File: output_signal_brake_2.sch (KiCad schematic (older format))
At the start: 37 parts

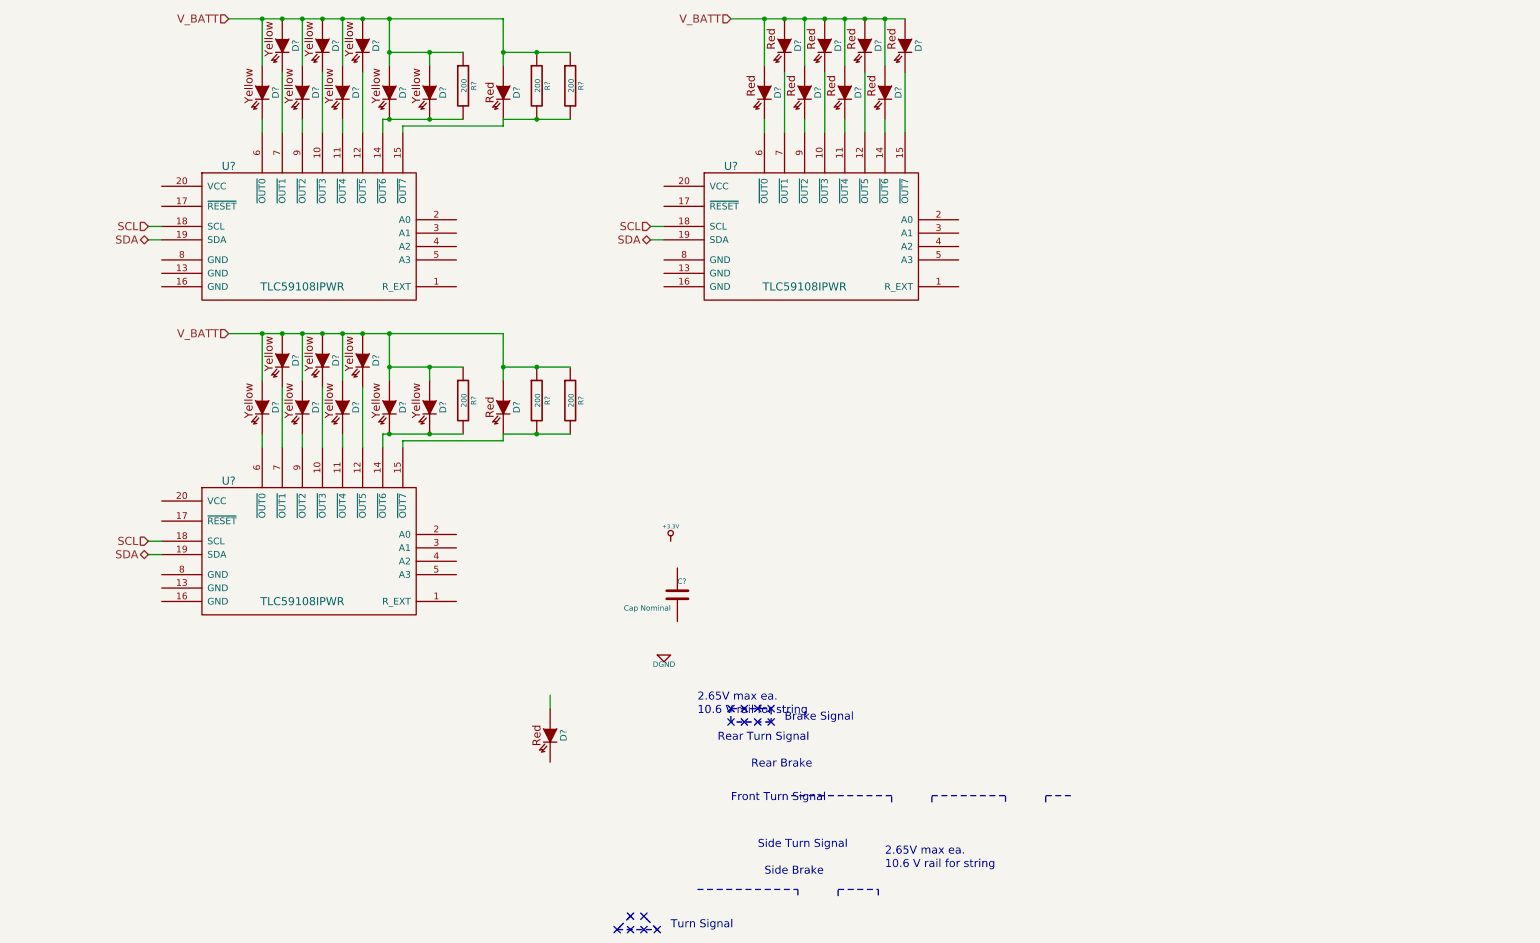
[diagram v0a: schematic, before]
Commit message: finished batt-current LED driver array over I2C
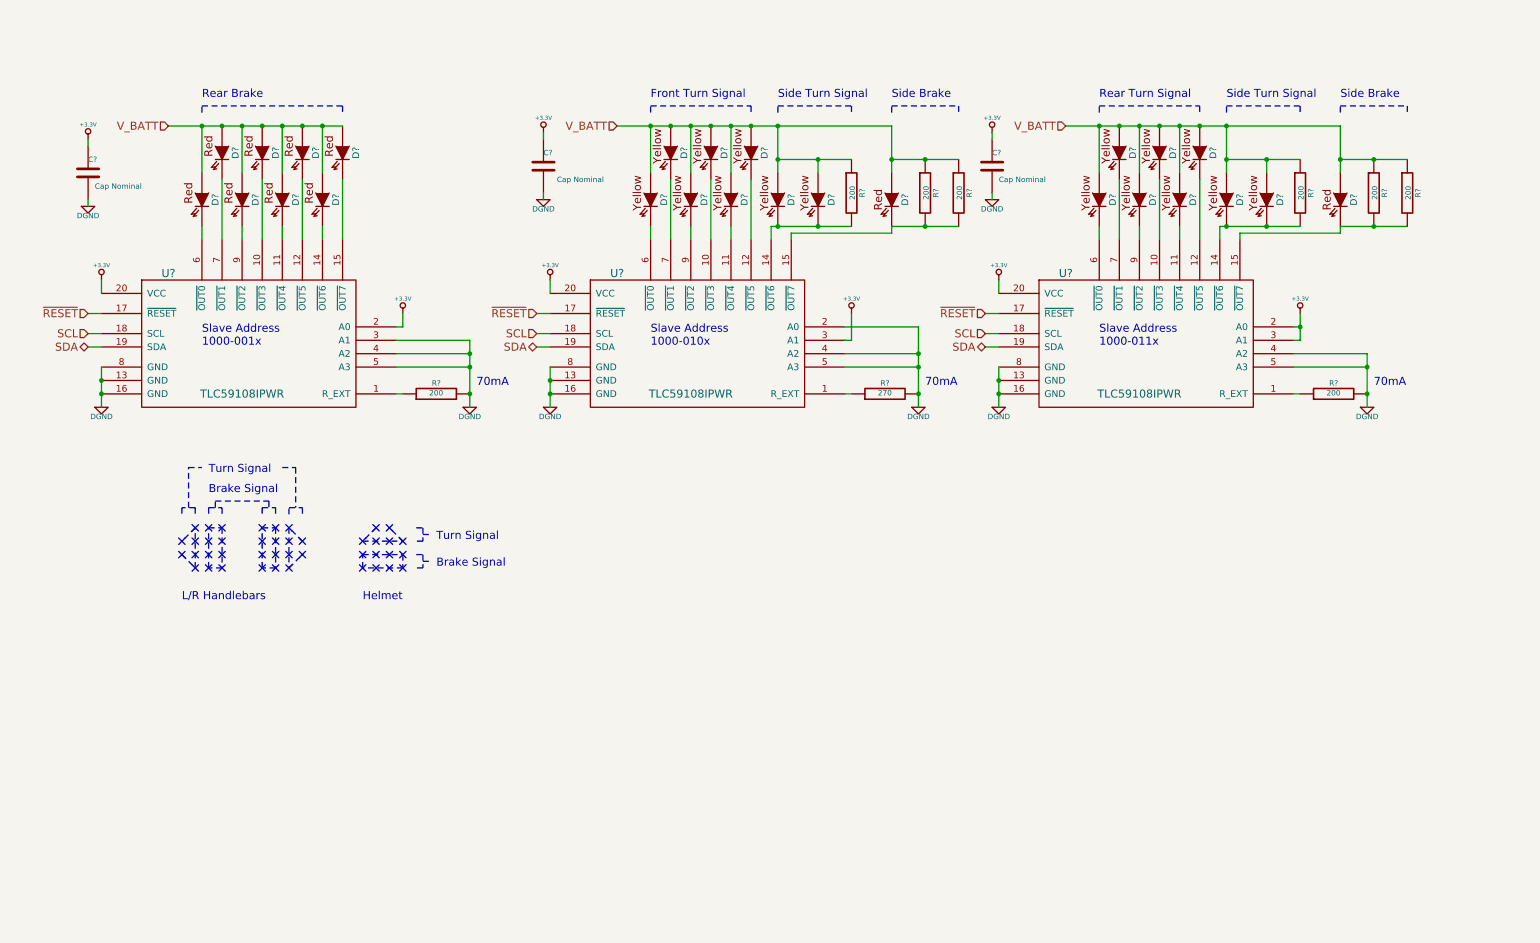
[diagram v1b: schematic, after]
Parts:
- removed D?: LR-A67F, ~, symbol LR-A67F
- added C? (x2): Cap Nominal, ~, symbol C
- added R?: 270, ~, symbol R
- added R? (x2): 200, ~, symbol R
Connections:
- net +3.3V: now also C?.1, U?.2 (A0), U?.2 (A0), U?.20 (VCC), U?.20 (VCC), U?.20 (VCC), U?.3 (A1), U?.3 (A1), C?.1, C?.1
- net DGND: now also C?.2, U?.13 (GND), U?.13 (GND), U?.13 (GND), U?.16 (GND), U?.16 (GND), U?.16 (GND), U?.2 (A0), U?.3 (A1), U?.4 (A2), U?.4 (A2), U?.4 (A2), U?.5 (A3), U?.5 (A3), U?.5 (A3), U?.8 (GND), U?.8 (GND), U?.8 (GND), C?.2, C?.2, R?.2, R?.2, R?.2
- net at U?.1 (R_EXT): now also R?.1 (x3)
- net ~RESET: now reaches U?.17 (~RESET)
- net ~RESET: now also U?.17 (~RESET), U?.17 (~RESET)
- no-connect marks 14 -> 42
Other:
- note added: "70mA"
- note added: "Helmet"
- note added: "L/R Handlebars"
- note added: "Slave Address\n1000-001x"
- note added: "Slave Address\n1000-010x"
- note added: "Slave Address\n1000-011x"
- note removed: "10.6 V rail for string"
- note removed: "2.65V max ea."
- moved on the sheet: C?, D?, R?, U?

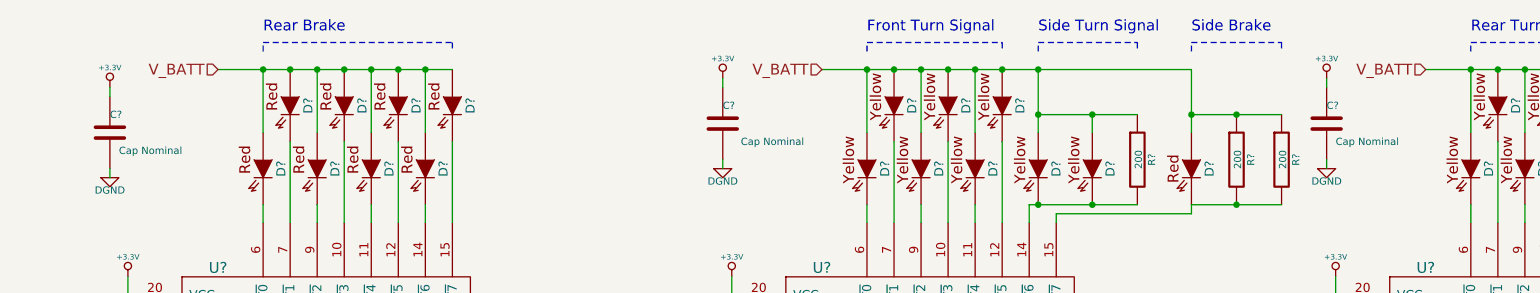
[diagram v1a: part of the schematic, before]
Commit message: added headlight sheet, led, dac
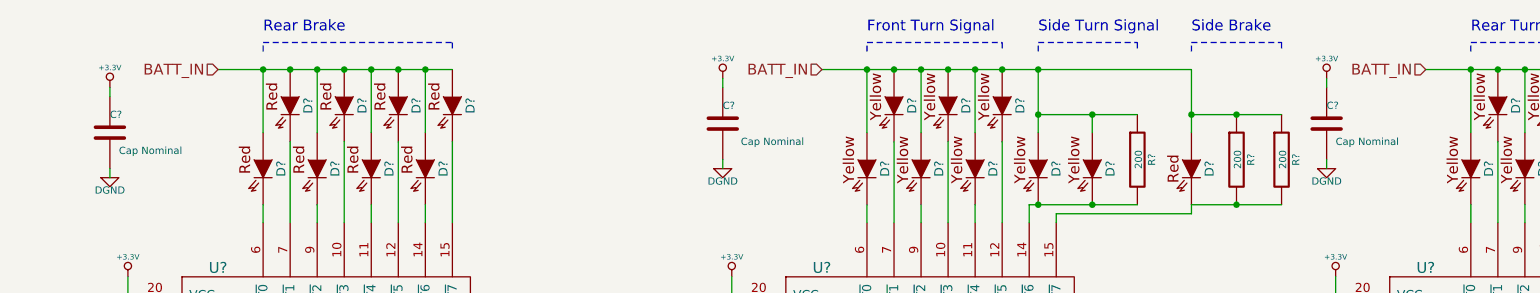
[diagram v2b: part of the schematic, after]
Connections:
- net V_BATT renamed BATT_IN
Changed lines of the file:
@@
 $Descr A4 11693 8268
 encoding utf-8
-Sheet 16 16
+Sheet 16 17
 Title ""
-Date "6 dec 2013"
+Date "7 dec 2013"
 Rev ""
 Comp ""
@@
 $EndComp
 Text HLabel 1500 1400 0    60   Input ~ 0
-V_BATT
+BATT_IN
 $Comp
 L R R?
@@
 	0    1    1    0
 $EndComp
-Text HLabel 8200 1400 0    60   Input ~ 0
-V_BATT
 $Comp
 L R R?
@@
 	0    1    1    0
 $EndComp
-Text HLabel 4850 1400 0    60   Input ~ 0
-V_BATT
 $Comp
 L R R?
@@
 Text Notes 3500 4700 0    60   ~ 0
 Brake Signal
+Text HLabel 4850 1400 0    60   Input ~ 0
+BATT_IN
+Text HLabel 8200 1400 0    60   Input ~ 0
+BATT_IN
 $EndSCHEMATC

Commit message: 2.5V Regulator finished.
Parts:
- added C? (x2): 22uF, ~, symbol CSMALL
- added C? (x2): 10nF, ~, symbol CSMALL
- added L?: 1uH, ~, symbol INDUCTOR
- added R?: 160k, ~, symbol RSMALL
- added R?: 75k, ~, symbol RSMALL
- added R?: 470k, ~, symbol RSMALL
- added U?: TPS62090, ~, symbol TPS62090
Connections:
- net labels added: +2.5V, +BATT, GND
- wire segments 97 -> 139
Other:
- note added: "Battery to 2.5V Buck Power Supply"

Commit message: added thermal pad to 2.5V, added some labels
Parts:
- R? (x2): value 200 -> 270
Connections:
- wire segments 139 -> 138
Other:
- note added: "Don't think we need this output\nor the pull up here. We aren't reading it...?"
- note added: "This needs to be connected."
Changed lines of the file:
@@
 P 10200 3400
 F 0 "R?" V 10280 3400 40  0000 C CNN
-F 1 "200" V 10207 3401 40  0000 C CNN
+F 1 "270" V 10207 3401 40  0000 C CNN
 F 2 "~" V 10130 3400 30  0000 C CNN
 F 3 "~" H 10200 3400 30  0000 C CNN
@@
 P 3500 3400
 F 0 "R?" V 3580 3400 40  0000 C CNN
-F 1 "200" V 3507 3401 40  0000 C CNN
+F 1 "270" V 3507 3401 40  0000 C CNN
 F 2 "~" V 3430 3400 30  0000 C CNN
 F 3 "~" H 3500 3400 30  0000 C CNN
@@
 Wire Wire Line
 	8450 5400 8350 5400
-$Comp
-L GND #PWR?
-U 1 1 52A69161
-P 8450 6250
-F 0 "#PWR?" H 8450 6250 30  0001 C CNN
-F 1 "GND" H 8450 6180 30  0001 C CNN
-F 2 "" H 8450 6250 60  0000 C CNN
-F 3 "" H 8450 6250 60  0000 C CNN
-	1    8450 6250
-	1    0    0    -1
-$EndComp
-Wire Wire Line
-	8350 6150 8450 6150
-Wire Wire Line
-	8450 6150 8450 6250
+Wire Wire Line
+	8350 6600 8350 6150
 $Comp
 L +BATT #PWR?
@@
 $Comp
 L GND #PWR?
-U 1 1 52A68AB3
-P 7700 6700
-F 0 "#PWR?" H 7700 6700 30  0001 C CNN
-F 1 "GND" H 7700 6630 30  0001 C CNN
-F 2 "" H 7700 6700 60  0000 C CNN
-F 3 "" H 7700 6700 60  0000 C CNN
-	1    7700 6700
-	1    0    0    -1
-$EndComp
-$Comp
-L GND #PWR?
 U 1 1 52A68AC2
 P 7500 6700
@@
 Wire Wire Line
 	7500 6600 7500 6700
-Wire Wire Line
-	7700 6600 7700 6700
 $Comp
 L +BATT #PWR?
@@
 $EndComp
 Connection ~ 9650 6050
+Wire Wire Line
+	7500 6600 8350 6600
+Connection ~ 7700 6600
+Connection ~ 7600 6600
+Text Notes 9100 6150 0    60   ~ 0
+Don't think we need this output\nor the pull up here. We aren't reading it...?
+Text Notes 5050 5800 0    60   ~ 0
+This needs to be connected.
 $EndSCHEMATC

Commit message: Minor fixes, labels, etc
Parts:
- removed R?: 470k, ~, symbol RSMALL
- added R?: Nominal, ~, symbol R
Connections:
- net labels added: PWR_EN, PWR_GOOD
- net labels removed: +BATT, GND
- wire segments 138 -> 133
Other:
- note removed: "This needs to be connected."
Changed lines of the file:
@@
 Sheet 15 18
 Title ""
-Date "10 dec 2013"
+Date "11 dec 2013"
 Rev ""
 Comp ""
@@
 	1    0    0    -1
 $EndComp
-Text HLabel 1500 1400 0    60   Input ~ 0
-BATT_IN
 $Comp
 L R R?
@@
 Text Notes 3500 4700 0    60   ~ 0
 Brake Signal
-Text HLabel 4850 1400 0    60   Input ~ 0
-BATT_IN
-Text HLabel 8200 1400 0    60   Input ~ 0
-BATT_IN
 $Comp
 L TPS62090 U?
@@
 Wire Wire Line
 	8350 6600 8350 6150
-$Comp
-L +BATT #PWR?
-U 1 1 52A69339
-P 8450 6000
-F 0 "#PWR?" H 8450 5950 20  0001 C CNN
-F 1 "+BATT" H 8450 6100 30  0000 C CNN
-F 2 "" H 8450 6000 60  0000 C CNN
-F 3 "" H 8450 6000 60  0000 C CNN
-	1    8450 6000
-	1    0    0    -1
-$EndComp
 Wire Wire Line
 	8350 6000 8450 6000
@@
 $EndComp
 $Comp
-L GND #PWR?
-U 1 1 52A68AC2
-P 7500 6700
-F 0 "#PWR?" H 7500 6700 30  0001 C CNN
-F 1 "GND" H 7500 6630 30  0001 C CNN
-F 2 "" H 7500 6700 60  0000 C CNN
-F 3 "" H 7500 6700 60  0000 C CNN
-	1    7500 6700
-	1    0    0    -1
-$EndComp
-$Comp
-L GND #PWR?
-U 1 1 52A68AD1
-P 6500 6300
-F 0 "#PWR?" H 6500 6300 30  0001 C CNN
-F 1 "GND" H 6500 6230 30  0001 C CNN
-F 2 "" H 6500 6300 60  0000 C CNN
-F 3 "" H 6500 6300 60  0000 C CNN
-	1    6500 6300
-	1    0    0    -1
-$EndComp
-$Comp
 L CSMALL C?
 U 1 1 52A68AEF
@@
 	1    0    0    -1
 $EndComp
-$Comp
-L GND #PWR?
-U 1 1 52A68B1C
-P 6400 5600
-F 0 "#PWR?" H 6400 5600 30  0001 C CNN
-F 1 "GND" H 6400 5530 30  0001 C CNN
-F 2 "" H 6400 5600 60  0000 C CNN
-F 3 "" H 6400 5600 60  0000 C CNN
-	1    6400 5600
-	1    0    0    -1
-$EndComp
 Connection ~ 8450 5250
 Wire Wire Line
@@
 Wire Wire Line
 	9400 5250 9400 5300
-Wire Wire Line
-	9650 5250 9650 5450
 Connection ~ 9400 5250
 Wire Wire Line
@@
 	9200 5700 8350 5700
 Connection ~ 9400 5550
-$Comp
-L GND #PWR?
-U 1 1 52A693F7
-P 9400 5900
-F 0 "#PWR?" H 9400 5900 30  0001 C CNN
-F 1 "GND" H 9400 5830 30  0001 C CNN
-F 2 "" H 9400 5900 60  0000 C CNN
-F 3 "" H 9400 5900 60  0000 C CNN
-	1    9400 5900
-	1    0    0    -1
-$EndComp
 Wire Wire Line
 	9400 5800 9400 5900
@@
 	9100 6050 10050 6050
 Wire Wire Line
-	9650 6050 9650 5650
-Wire Wire Line
-	6000 5250 6850 5250
-Wire Wire Line
-	6800 5250 6800 5550
-Wire Wire Line
-	6800 5400 6850 5400
-Connection ~ 6800 5250
-Wire Wire Line
-	6800 5550 6850 5550
-Connection ~ 6800 5400
+	6250 5250 6850 5250
 Wire Wire Line
 	6400 5300 6400 5250
 Connection ~ 6400 5250
 Wire Wire Line
-	6400 5500 6400 5600
+	6400 5500 6400 5550
 Wire Wire Line
 	6750 5850 6850 5850
@@
 Wire Wire Line
 	7500 6600 7500 6700
-$Comp
-L +BATT #PWR?
-U 1 1 52A6A360
-P 6000 5200
-F 0 "#PWR?" H 6000 5150 20  0001 C CNN
-F 1 "+BATT" H 6000 5300 30  0000 C CNN
-F 2 "" H 6000 5200 60  0000 C CNN
-F 3 "" H 6000 5200 60  0000 C CNN
-	1    6000 5200
-	1    0    0    -1
-$EndComp
-Wire Wire Line
-	6000 5250 6000 5200
-$Comp
-L GND #PWR?
-U 1 1 52A6A483
-P 9900 5550
-F 0 "#PWR?" H 9900 5550 30  0001 C CNN
-F 1 "GND" H 9900 5480 30  0001 C CNN
-F 2 "" H 9900 5550 60  0000 C CNN
-F 3 "" H 9900 5550 60  0000 C CNN
-	1    9900 5550
-	1    0    0    -1
-$EndComp
 Wire Wire Line
 	9900 5500 9900 5550
@@
 Wire Wire Line
 	10050 5250 10050 5200
-Text HLabel 1500 850  0    60   Input ~ 0
-BATT_IN
-$Comp
-L +BATT #PWR?
-U 1 1 52A6AAF7
-P 1650 750
-F 0 "#PWR?" H 1650 700 20  0001 C CNN
-F 1 "+BATT" H 1650 850 30  0000 C CNN
-F 2 "" H 1650 750 60  0000 C CNN
-F 3 "" H 1650 750 60  0000 C CNN
-	1    1650 750
-	1    0    0    -1
-$EndComp
-Wire Wire Line
-	1650 750  1650 850
-Wire Wire Line
-	1650 850  1500 850
-Wire Wire Line
-	6850 5700 5700 5700
 Text Notes 6800 4750 0    60   ~ 0
 Battery to 2.5V Buck Power Supply
+$Comp
+L RSMALL R?
+U 1 1 52A6B2C1
+P 9400 5700
+F 0 "R?" V 9450 5700 30  0000 C TNN
+F 1 "75k" V 9350 5700 30  0000 C BNN
+F 2 "~" H 9400 5735 60  0000 C CNN
+F 3 "~" H 9400 5735 60  0000 C CNN
+	1    9400 5700
+	1    0    0    -1
+$EndComp
+Connection ~ 9650 6050
+Wire Wire Line
+	7500 6600 8350 6600
+Connection ~ 7700 6600
+Connection ~ 7600 6600
+Text Notes 9100 6600 0    60   ~ 0
+Don't think we need this output\nor the pull up here. We aren't reading it...?
+Text HLabel 6250 5250 0    60   Input ~ 0
+BATT_IN
+Text HLabel 8450 6000 2    60   Input ~ 0
+BATT_IN
+$Comp
+L DGND #PWR?
+U 1 1 52A7FDF9
+P 6400 5550
+F 0 "#PWR?" H 6400 5550 40  0001 C CNN
+F 1 "DGND" H 6400 5480 40  0000 C CNN
+F 2 "" H 6400 5550 60  0000 C CNN
+F 3 "" H 6400 5550 60  0000 C CNN
+	1    6400 5550
+	1    0    0    -1
+$EndComp
+$Comp
+L DGND #PWR?
+U 1 1 52A7FDFF
+P 6500 6300
+F 0 "#PWR?" H 6500 6300 40  0001 C CNN
+F 1 "DGND" H 6500 6230 40  0000 C CNN
+F 2 "" H 6500 6300 60  0000 C CNN
+F 3 "" H 6500 6300 60  0000 C CNN
+	1    6500 6300
+	1    0    0    -1
+$EndComp
+$Comp
+L DGND #PWR?
+U 1 1 52A7FE05
+P 7500 6700
+F 0 "#PWR?" H 7500 6700 40  0001 C CNN
+F 1 "DGND" H 7500 6630 40  0000 C CNN
+F 2 "" H 7500 6700 60  0000 C CNN
+F 3 "" H 7500 6700 60  0000 C CNN
+	1    7500 6700
+	1    0    0    -1
+$EndComp
+$Comp
+L DGND #PWR?
+U 1 1 52A7FE0B
+P 9400 5900
+F 0 "#PWR?" H 9400 5900 40  0001 C CNN
+F 1 "DGND" H 9400 5830 40  0000 C CNN
+F 2 "" H 9400 5900 60  0000 C CNN
+F 3 "" H 9400 5900 60  0000 C CNN
+	1    9400 5900
+	1    0    0    -1
+$EndComp
+$Comp
+L DGND #PWR?
+U 1 1 52A7FE11
+P 9900 5550
+F 0 "#PWR?" H 9900 5550 40  0001 C CNN
+F 1 "DGND" H 9900 5480 40  0000 C CNN
+F 2 "" H 9900 5550 60  0000 C CNN
+F 3 "" H 9900 5550 60  0000 C CNN
+	1    9900 5550
+	1    0    0    -1
+$EndComp
+$Comp
+L +2.5V #PWR?
+U 1 1 52A802AB
+P 1500 1400
+F 0 "#PWR?" H 1500 1350 20  0001 C CNN
+F 1 "+2.5V" H 1500 1500 30  0000 C CNN
+F 2 "" H 1500 1400 60  0000 C CNN
+F 3 "" H 1500 1400 60  0000 C CNN
+	1    1500 1400
+	1    0    0    -1
+$EndComp
+$Comp
+L +2.5V #PWR?
+U 1 1 52A802B1
+P 4850 1400
+F 0 "#PWR?" H 4850 1350 20  0001 C CNN
+F 1 "+2.5V" H 4850 1500 30  0000 C CNN
+F 2 "" H 4850 1400 60  0000 C CNN
+F 3 "" H 4850 1400 60  0000 C CNN
+	1    4850 1400
+	1    0    0    -1
+$EndComp
+$Comp
+L +2.5V #PWR?
+U 1 1 52A802B7
+P 8200 1400
+F 0 "#PWR?" H 8200 1350 20  0001 C CNN
+F 1 "+2.5V" H 8200 1500 30  0000 C CNN
+F 2 "" H 8200 1400 60  0000 C CNN
+F 3 "" H 8200 1400 60  0000 C CNN
+	1    8200 1400
+	1    0    0    -1
+$EndComp
+$Comp
+L R R?
+U 1 1 52A80325
+P 9650 5550
+F 0 "R?" V 9730 5550 40  0000 C CNN
+F 1 "Nominal" V 9657 5551 40  0000 C CNN
+F 2 "~" V 9580 5550 30  0000 C CNN
+F 3 "~" H 9650 5550 30  0000 C CNN
+	1    9650 5550
+	1    0    0    -1
+$EndComp
+Wire Wire Line
+	9650 5250 9650 5300
+Wire Wire Line
+	9650 5800 9650 6050
 $Comp
 L RSMALL R?
@@
 	1    0    0    -1
 $EndComp
-$Comp
-L RSMALL R?
-U 1 1 52A6B2C1
-P 9400 5700
-F 0 "R?" V 9450 5700 30  0000 C TNN
-F 1 "75k" V 9350 5700 30  0000 C BNN
-F 2 "~" H 9400 5735 60  0000 C CNN
-F 3 "~" H 9400 5735 60  0000 C CNN
-	1    9400 5700
-	1    0    0    -1
-$EndComp
-$Comp
-L RSMALL R?
-U 1 1 52A6B2D5
-P 9650 5550
-F 0 "R?" V 9700 5550 30  0000 C TNN
-F 1 "470k" V 9600 5550 30  0000 C BNN
-F 2 "~" H 9650 5585 60  0000 C CNN
-F 3 "~" H 9650 5585 60  0000 C CNN
-	1    9650 5550
-	1    0    0    -1
-$EndComp
-Connection ~ 9650 6050
-Wire Wire Line
-	7500 6600 8350 6600
-Connection ~ 7700 6600
-Connection ~ 7600 6600
-Text Notes 9100 6150 0    60   ~ 0
-Don't think we need this output\nor the pull up here. We aren't reading it...?
-Text Notes 5050 5800 0    60   ~ 0
-This needs to be connected.
+Text HLabel 10050 6050 2    60   Output ~ 0
+PWR_GOOD
+Wire Wire Line
+	6850 5250 6850 5550
+Connection ~ 6850 5400
+Text HLabel 6250 5700 0    60   Input ~ 0
+PWR_EN
+Wire Wire Line
+	6250 5700 6850 5700
 $EndSCHEMATC
